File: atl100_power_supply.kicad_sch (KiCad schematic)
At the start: 3 parts, among them U1 XL4005

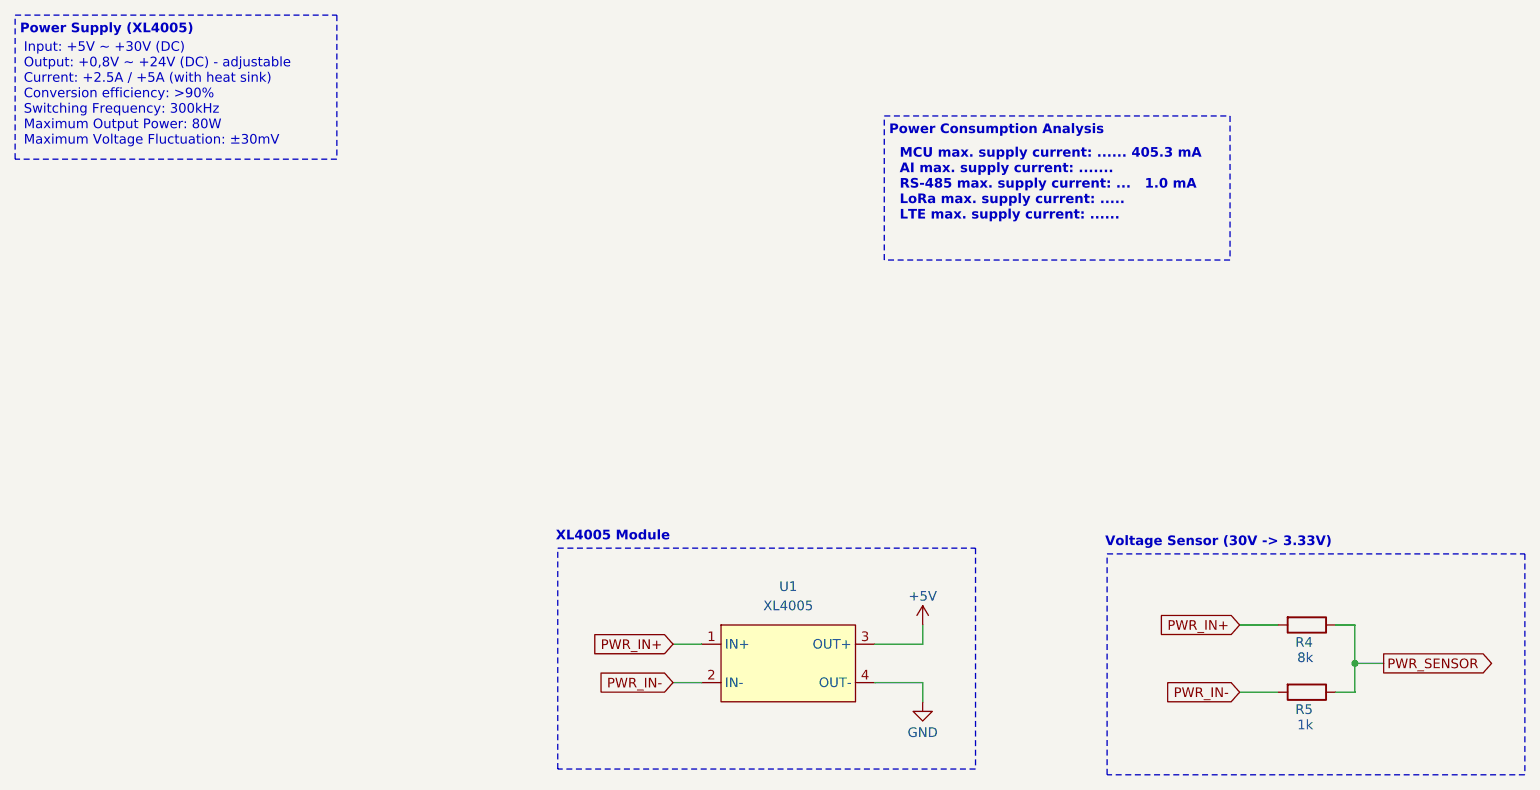
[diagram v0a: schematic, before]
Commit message: feat: Main board schematic updated
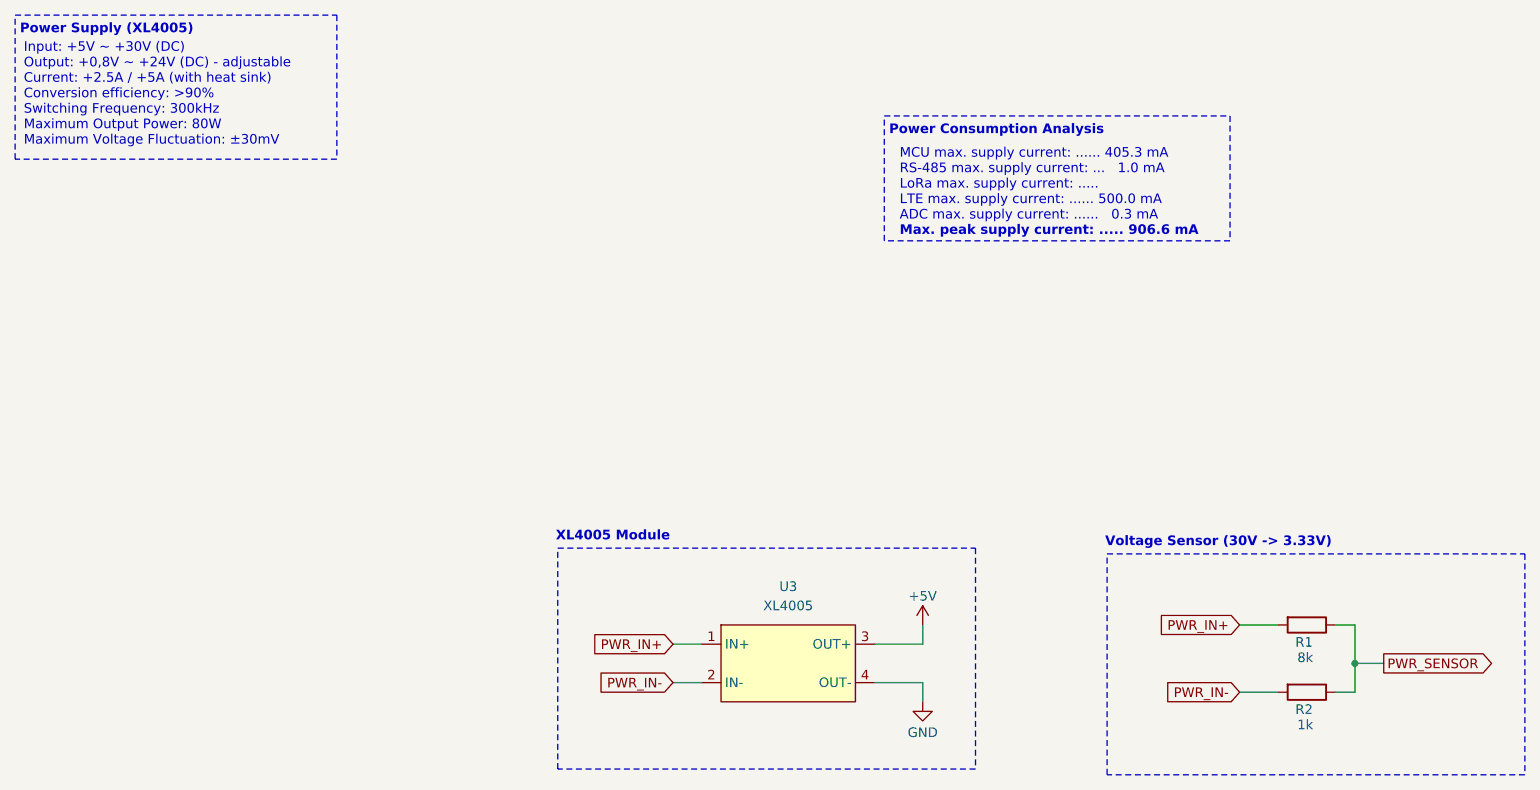
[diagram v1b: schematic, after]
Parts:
- renumbered R4 to R1, R5 to R2, U1 to U3
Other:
- note added: "MCU max. supply current: ...... 405.3 mA RS-485 max. supply current: ... 1.0 mA LoRa max. supply current: ..... LTE max. supply current: ...... 500.0 mA ADC max. supply current: ...... 0.3 mA"
- note added: "Max. peak supply current: ..... 906.6 mA"
- note removed: "MCU max. supply current: ...... 405.3 mA AI max. supply current: ....... RS-485 max. supply current: ... 1.0 mA LoRa max. supply current: ..... LTE max. supply current: ......"
- title: ATL-100 (Multiparametric Station) -> ATL-100 (Multiparametric Station) - Main Board
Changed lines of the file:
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@@
 	(paper "A4")
 	(title_block
-		(title "ATL-100 (Multiparametric Station)")
-		(date "2025-06-01")
+		(title "ATL-100 (Multiparametric Station) - Main Board")
+		(date "2025-06-02")
 		(rev "v0.2.0")
 		(company "AgroTechLab (Agribusiness Technology Development Laboratory)")
@@
 	(rectangle
 		(start 128.27 26.67)
-		(end 173.99 45.72)
+		(end 173.99 43.18)
 		(stroke
 			(width 0)
@@
 		)
 	)
-	(text "MCU max. supply current: ...... 405.3 mA\nAI max. supply current: .......\nRS-485 max. supply current: ...   1.0 mA\nLoRa max. supply current: .....\nLTE max. supply current: ......"
+	(text "Max. peak supply current: ..... 906.6 mA"
+		(exclude_from_sim no)
+		(at 130.302 42.672 0)
+		(effects
+			(font
+				(face "Courier New")
+				(size 1.27 1.27)
+				(bold yes)
+				(color 9 23 255 1)
+			)
+			(justify left bottom)
+		)
+	)
+	(text "MCU max. supply current: ...... 405.3 mA\nRS-485 max. supply current: ...   1.0 mA\nLoRa max. supply current: .....\nLTE max. supply current: ...... 500.0 mA\nADC max. supply current: ......   0.3 mA"
 		(exclude_from_sim no)
 		(at 130.302 40.64 0)
@@
 				(face "Courier New")
 				(size 1.27 1.27)
-				(bold yes)
 				(color 9 23 255 1)
 			)
@@
 		(on_board yes)
 		(dnp no)
-		(property "Reference" "#PWR09"
+		(property "Reference" "#PWR016"
 			(at 133.35 97.79 0)
 			(effects
@@
 			(project "atl100_tht"
 				(path "/9f25808e-b525-4dd9-b9a0-a085d29b6aa9/eaaf634d-252e-431d-b15b-fb2b1eecc847"
-					(reference "#PWR09")
+					(reference "#PWR016")
 					(unit 1)
 				)
@@
 		(dnp no)
 		(fields_autoplaced yes)
-		(property "Reference" "U1"
+		(property "Reference" "U3"
 			(at 115.57 88.9 0)
 			(effects
@@
 			(project ""
 				(path "/9f25808e-b525-4dd9-b9a0-a085d29b6aa9/eaaf634d-252e-431d-b15b-fb2b1eecc847"
-					(reference "U1")
+					(reference "U3")
 					(unit 1)
 				)
@@
 		(on_board yes)
 		(dnp no)
-		(property "Reference" "R4"
+		(property "Reference" "R1"
 			(at 182.626 96.266 90)
 			(effects
@@
 			(project "atl100_tht"
 				(path "/9f25808e-b525-4dd9-b9a0-a085d29b6aa9/eaaf634d-252e-431d-b15b-fb2b1eecc847"
-					(reference "R4")
+					(reference "R1")
 					(unit 1)
 				)
@@
 		(on_board yes)
 		(dnp no)
-		(property "Reference" "R5"
+		(property "Reference" "R2"
 			(at 182.626 105.156 90)
 			(effects
@@
 			(project "atl100_tht"
 				(path "/9f25808e-b525-4dd9-b9a0-a085d29b6aa9/eaaf634d-252e-431d-b15b-fb2b1eecc847"
-					(reference "R5")
+					(reference "R2")
 					(unit 1)
 				)
@@
 		(on_board yes)
 		(dnp no)
-		(property "Reference" "#PWR010"
+		(property "Reference" "#PWR017"
 			(at 133.35 110.49 0)
 			(effects
@@
 			(project "atl100_tht"
 				(path "/9f25808e-b525-4dd9-b9a0-a085d29b6aa9/eaaf634d-252e-431d-b15b-fb2b1eecc847"
-					(reference "#PWR010")
+					(reference "#PWR017")
 					(unit 1)
 				)

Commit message: feat: Updated to v0.2.0
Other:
- note added: "MCU max. supply current: ...... 405.3 mA RS-485 max. supply current: ... 1.0 mA LoRa max. supply current: ..... 120.0 mA LTE max. supply current: ...... 500.0 mA ADC max. supply current: ...... 0.3 mA"
- note removed: "MCU max. supply current: ...... 405.3 mA RS-485 max. supply current: ... 1.0 mA LoRa max. supply current: ..... LTE max. supply current: ...... 500.0 mA ADC max. supply current: ...... 0.3 mA"
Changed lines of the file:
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@@
 	(title_block
 		(title "ATL-100 (Multiparametric Station) - Main Board")
-		(date "2025-06-02")
+		(date "2025-06-05")
 		(rev "v0.2.0")
 		(company "AgroTechLab (Agribusiness Technology Development Laboratory)")
@@
 		)
 	)
-	(text "MCU max. supply current: ...... 405.3 mA\nRS-485 max. supply current: ...   1.0 mA\nLoRa max. supply current: .....\nLTE max. supply current: ...... 500.0 mA\nADC max. supply current: ......   0.3 mA"
+	(text "MCU max. supply current: ...... 405.3 mA\nRS-485 max. supply current: ...   1.0 mA\nLoRa max. supply current: ..... 120.0 mA\nLTE max. supply current: ...... 500.0 mA\nADC max. supply current: ......   0.3 mA"
 		(exclude_from_sim no)
 		(at 130.302 40.64 0)
